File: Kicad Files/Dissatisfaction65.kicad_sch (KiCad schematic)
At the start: 139 parts, among them SW1 Rotary_Encoder_Switch, SW2 SW_SPST, U1 Pro_Micro_ProMicro, U2 74HC4515, U3 SSD1306_I2C

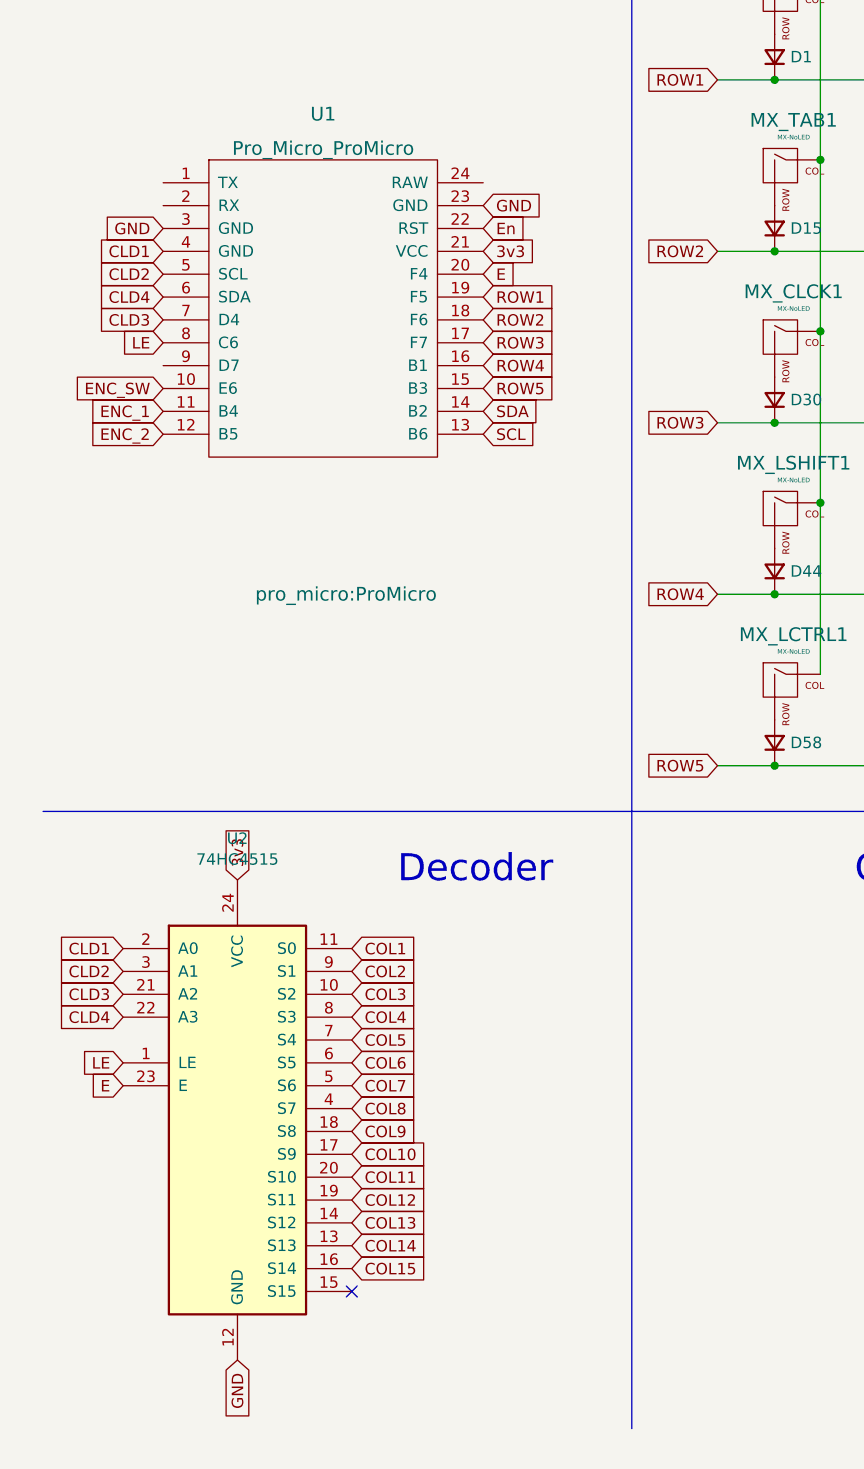
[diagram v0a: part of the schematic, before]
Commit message: Adding updated schematic. This is the scheamtic I used to generate the pdf with an addition bold comment by the decoder that we must use the 74HC4514
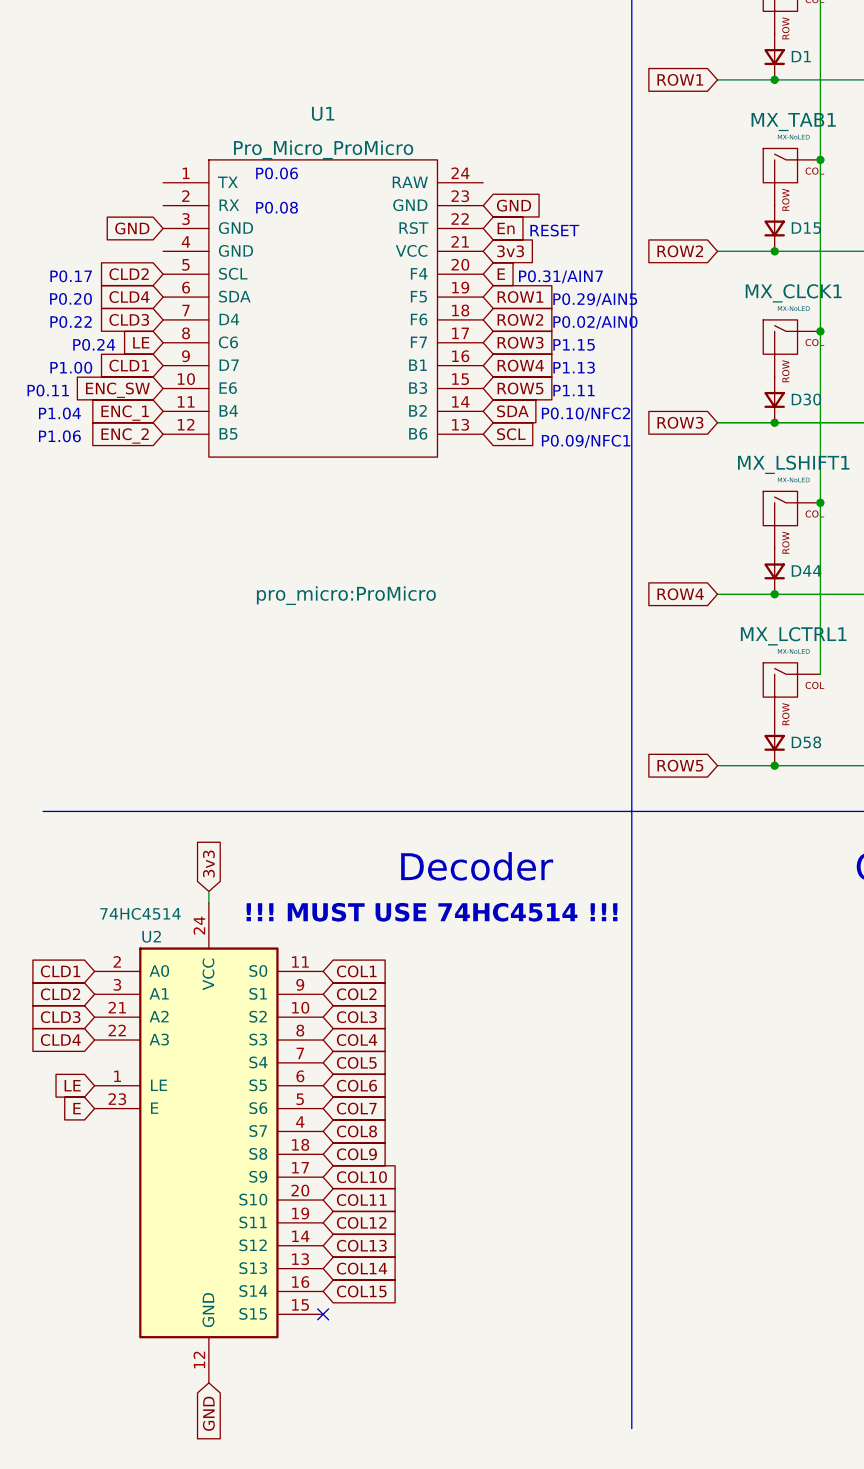
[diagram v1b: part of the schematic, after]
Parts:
- U2: value 74HC4515 -> 74HC4514
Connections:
- net CLD1: now also U1.9 (D7); no longer U1.4 (GND)
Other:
- note added: "!!! MUST USE 74HC4514 !!!"
- note added: "P0.02/AIN0"
- note added: "P0.06"
- note added: "P0.08"
- note added: "P0.09/NFC1"
- note added: "P0.10/NFC2"
- note added: "P0.11"
- note added: "P0.17"
- note added: "P0.20"
- note added: "P0.22"
- note added: "P0.24"
- note added: "P0.29/AIN5"
- note added: "P0.31/AIN7"
- note added: "P1.00"
- note added: "P1.04"
- note added: "P1.06"
- note added: "P1.11"
- note added: "P1.13"
- note added: "P1.15"
- note added: "RESET"
- moved on the sheet: U2
